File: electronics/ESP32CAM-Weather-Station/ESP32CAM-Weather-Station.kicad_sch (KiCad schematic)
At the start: 63 parts, among them IC1 BME688, IC2 SGP41-D-R4, IC3 VEML7700-TT, IC4 BQ24093DGQR, IC5 BQ29707DSET, IC6 MCP3426A0T-E_SN, IC7 TPS63070RNMR, J1 B4B-PH-SM4-TB_LF__SN_, J10 Conn_01x02_Pin, J2 B4B-PH-SM4-TB_LF__SN_, J3 B4B-PH-SM4-TB_LF__SN_, J4 B4B-PH-SM4-TB_LF__SN_, J5 B4B-PH-SM4-TB_LF__SN_, J6 XT30UPB-M, J7 Conn_01x02_Pin, J9 Conn_01x02_Pin, Q1 SIHLL110TR-GE3, Q2 CSD16406Q3, Q3 CSD16406Q3, U1 ESP32-CAM, U2 TPS631000DRLR

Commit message: [WIP] Added transient protection and mounting holes.
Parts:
- added D10, D11, D12, D13, D6, D7, D8, D9: ESDZV5H-1BU2, ESDZV5H-1BU2:ESDZV5H1BU2, symbol ESDZV5H-1BU2:ESDZV5H-1BU2
- added D5: SMBJ20CA-TR, SMBJ20CA-TR:DIONM5436X265N, symbol SMBJ20CA-TR:SMBJ20CA-TR
- added H2, H3, H4, H6: MountingHole, MountingHole:MountingHole_3.2mm_M3_Pad_Via, symbol Mechanical:MountingHole
- added H5: MountingHole_Pad, MountingHole:MountingHole_3.2mm_M3_DIN965_Pad, symbol Mechanical:MountingHole_Pad
- added J8: Conn_01x02_Pin, Connector_PinHeader_2.54mm:PinHeader_1x02_P2.54mm_Vertical, symbol Connector:Conn_01x02_Pin
- added U3: GDT25-07-S1-RP, GDT25-07-S1-RP:GDT2507S1RP, symbol GDT25-07-S1-RP:GDT25-07-S1-RP
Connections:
- net +3.3V: now also D10.2, D6.2, D7.2, D8.2
- net +VBAT: now also D13.2
- net +VBAT_UNFUSED: now also J8.1 (Pin_1)
- net GND: now also J6.N, D10.1, D11.1, D12.1, D13.1, D5.2, D6.1, D7.1, D8.1, D9.2, H5.1, J8.2 (Pin_2), U3.2
- net I2C_SDA: now also D11.2, D12.2
- net +VSOLAR: now reaches J6.P
- net +VSOLAR: now also R5.2, D5.1, U3.1
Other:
- note added: "Direct Battery and Solar Regulator Bypass"
- note added: "I2C Pullups and Protection"
- note added: "Mounting Holes and Earthing"
- note added: "Solar Protection"
- note removed: "Direct Battery and LDO Input Connection"
- note removed: "I2C Pullups"
- moved on the sheet: F1, H1, IC3, IC6, IC7, J10, J6, J9, R10, R11, R12, R13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

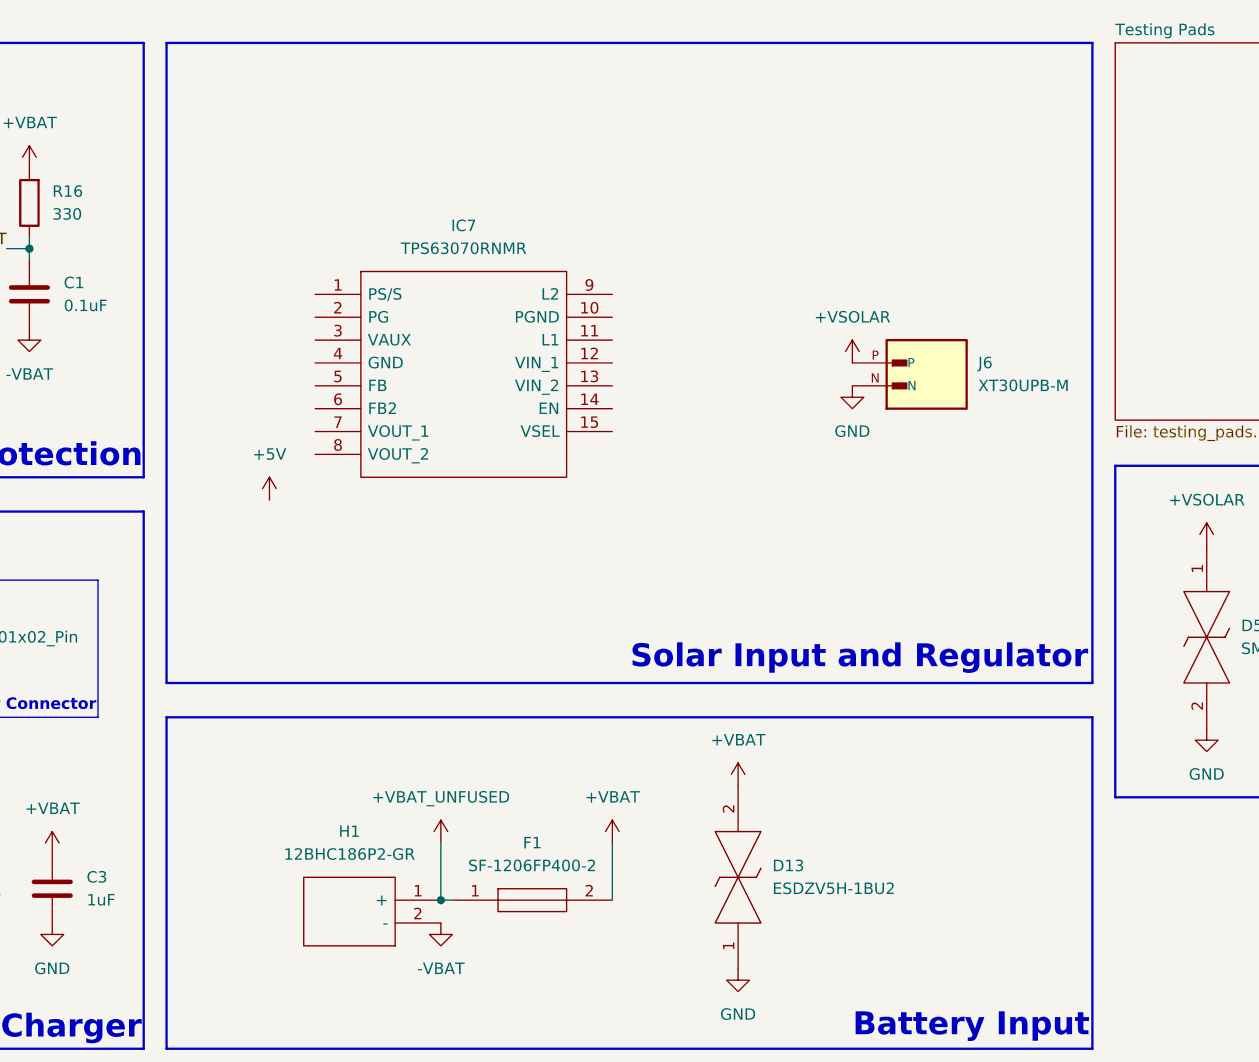
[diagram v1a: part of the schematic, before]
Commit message: [WIP] Routed solar input regulator.
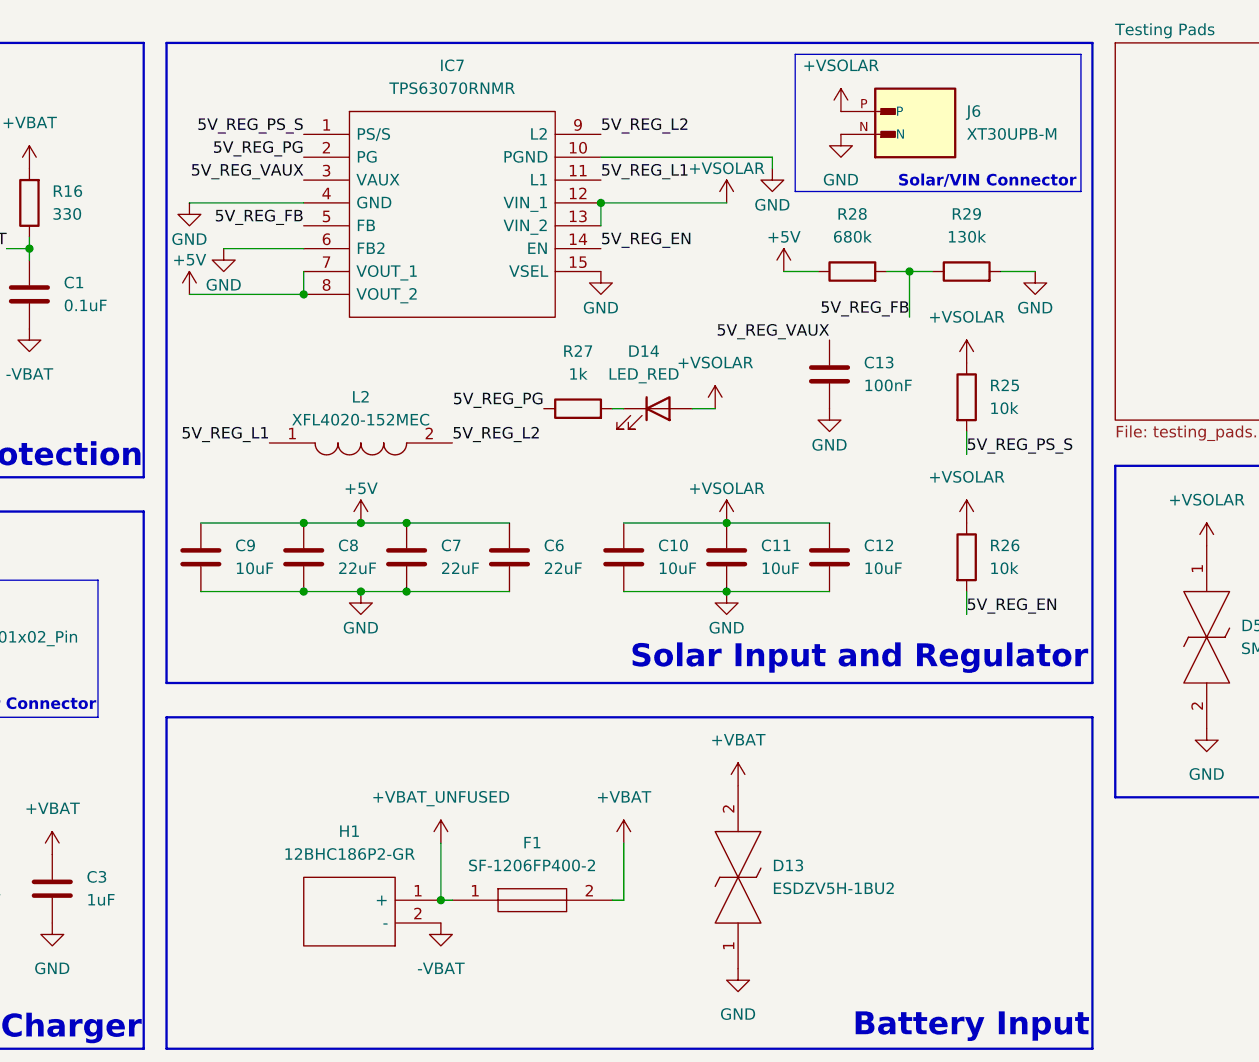
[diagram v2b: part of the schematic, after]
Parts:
- added C10, C9: 10uF, Capacitor_SMD:C_0603_1608Metric_Pad1.08x0.95mm_HandSolder, symbol Device:C
- added C11, C12: 10uF, Capacitor_SMD:C_0805_2012Metric_Pad1.18x1.45mm_HandSolder, symbol Device:C
- added C13: 100nF, Capacitor_SMD:C_0603_1608Metric_Pad1.08x0.95mm_HandSolder, symbol Device:C
- added C6, C7, C8: 22uF, Capacitor_SMD:C_0805_2012Metric_Pad1.18x1.45mm_HandSolder, symbol Device:C
- added D14: LED_RED, LED_SMD:LED_0805_2012Metric_Pad1.15x1.40mm_HandSolder, symbol Device:LED
- added L2: XFL4020-152MEC, XFL4020152MEC, symbol XFL4020-152MEC:XFL4020-152MEC
- added R25, R26: 10k, Resistor_SMD:R_0805_2012Metric_Pad1.20x1.40mm_HandSolder, symbol Device:R
- added R27: 1k, Resistor_SMD:R_0805_2012Metric_Pad1.20x1.40mm_HandSolder, symbol Device:R
- added R28: 680k, Resistor_SMD:R_0805_2012Metric_Pad1.20x1.40mm_HandSolder, symbol Device:R
- added R29: 130k, Resistor_SMD:R_0805_2012Metric_Pad1.20x1.40mm_HandSolder, symbol Device:R
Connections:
- net +5V: now also IC7.7 (VOUT_1), IC7.8 (VOUT_2), C6.1, C7.1, C8.1, C9.1, R28.1
- net +VSOLAR: now also IC7.12 (VIN_1), IC7.13 (VIN_2), C10.1, C11.1, C12.1, D14.2 (A), R25.1, R26.1
- net GND: now also IC7.10 (PGND), IC7.15 (VSEL), IC7.4 (GND), IC7.6 (FB2), C10.2, C11.2, C12.2, C13.1, C6.2, C7.2, C8.2, C9.2, R29.2
- net 5V_REG_PS_S: now reaches IC7.1 (PS/S)
- net 5V_REG_PS_S: now also R25.2
- net 5V_REG_L1: now reaches IC7.11 (L1)
- net 5V_REG_L1: now also L2.1
- net 5V_REG_EN: now reaches IC7.14 (EN)
- net 5V_REG_EN: now also R26.2
- net 5V_REG_PG: now reaches IC7.2 (PG)
- net 5V_REG_PG: now also R27.1
- net 5V_REG_VAUX: now reaches IC7.3 (VAUX)
- net 5V_REG_VAUX: now also C13.2
- net 5V_REG_FB: now reaches IC7.5 (FB)
- net 5V_REG_FB: now also R28.2, R29.1
- net 5V_REG_L2: now reaches IC7.9 (L2)
- net 5V_REG_L2: now also L2.2
- new net: D14.1 (K), R27.2
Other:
- note added: "Solar/VIN Connector"
- moved on the sheet: IC7, J6

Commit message: [WIP] Routed ADC and buzzer.
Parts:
- added C14: 10uF, Capacitor_SMD:C_0805_2012Metric_Pad1.18x1.45mm_HandSolder, symbol Device:C
- added C15: 100nF, Capacitor_SMD:C_0603_1608Metric_Pad1.08x0.95mm_HandSolder, symbol Device:C
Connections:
- net +3.3V: now also D9.1, IC6.3 (VDD), LS1.1 (+), C14.1, C15.2
- net GND: now also IC6.2 (CH1-), IC6.6 (VSS), IC6.8 (CH2-), Q1.3 (S), C14.2, C15.1
- net I2C_SCL: now also IC6.5 (SCL)
- net I2C_SDA: now also IC6.4 (SDA)
- net VBAT_SNS: now also IC6.1 (CH1+)
- net VSOLAR_SNS: now also IC6.7 (CH2+)
- net BUZZER_N: now reaches LS1.2 (-)
- net BUZZER_N: now also Q1.2 (D_1), Q1.4 (D_2)
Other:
- moved on the sheet: D1, D2, D6, IC6, JP1, JP2, JP3, R1, R2

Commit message: [WIP] Routed light sensor.
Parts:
- added C16: 10uF, Capacitor_SMD:C_0805_2012Metric_Pad1.18x1.45mm_HandSolder, symbol Device:C
- added C17: 100nF, Capacitor_SMD:C_0603_1608Metric_Pad1.08x0.95mm_HandSolder, symbol Device:C
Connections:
- net +3.3V: now also IC3.2 (VDD), C16.1, C17.2
- net GND: now also IC3.3 (GND), C16.2, C17.1
- net I2C_SCL: now also IC3.1 (SCL)
- net I2C_SDA: now also IC3.4 (SDA)
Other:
- moved on the sheet: D9

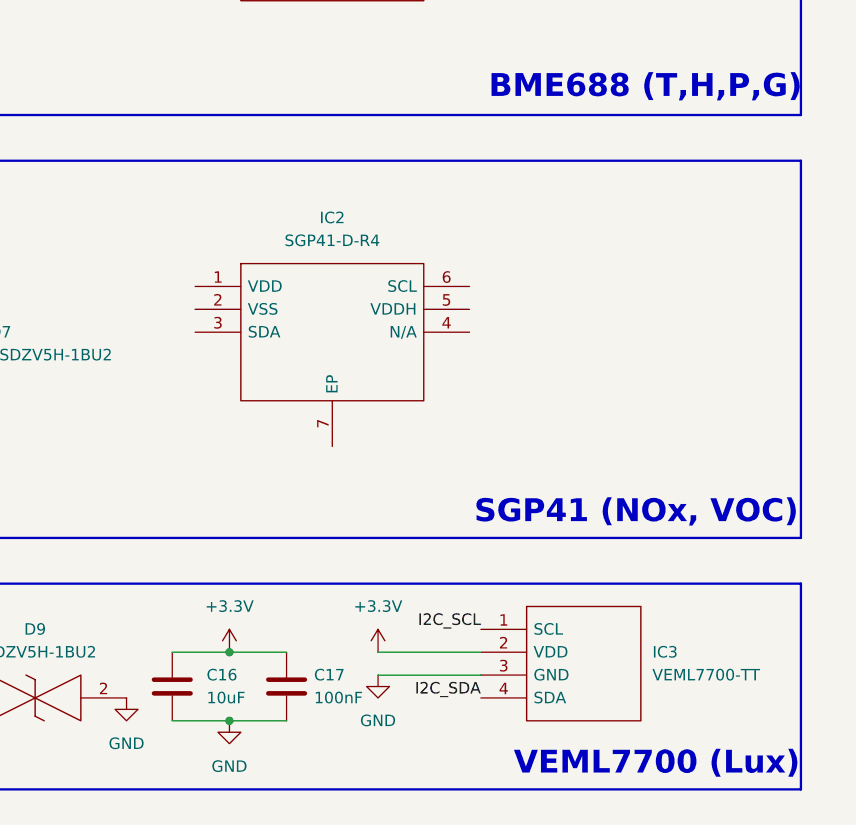
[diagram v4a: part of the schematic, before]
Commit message: [WIP] Routed SGP41.
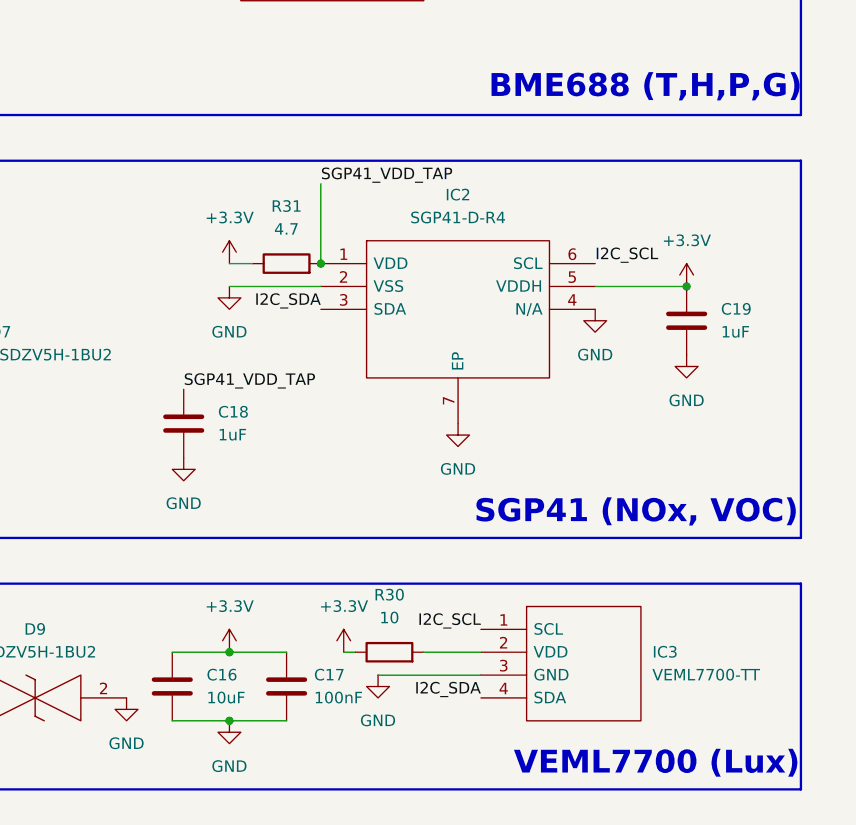
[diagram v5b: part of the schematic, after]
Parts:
- added C18, C19: 1uF, Capacitor_SMD:C_0805_2012Metric_Pad1.18x1.45mm_HandSolder, symbol Device:C
- added R30: 10, Resistor_SMD:R_0805_2012Metric_Pad1.20x1.40mm_HandSolder, symbol Device:R
- added R31: 4.7, Resistor_SMD:R_0805_2012Metric_Pad1.20x1.40mm_HandSolder, symbol Device:R
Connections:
- net +3.3V: now also IC2.5 (VDDH), C19.1, R30.1, R31.1; no longer IC3.2 (VDD)
- net GND: now also IC2.2 (VSS), IC2.4 (N/A), IC2.7 (EP), C18.2, C19.2
- net I2C_SCL: now also IC2.6 (SCL)
- net I2C_SDA: now also IC2.3 (SDA)
- net SGP41_VDD_TAP: now reaches IC2.1 (VDD)
- net SGP41_VDD_TAP: now also C18.1, R31.2
- new net: IC3.2 (VDD), R30.2
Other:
- moved on the sheet: IC2

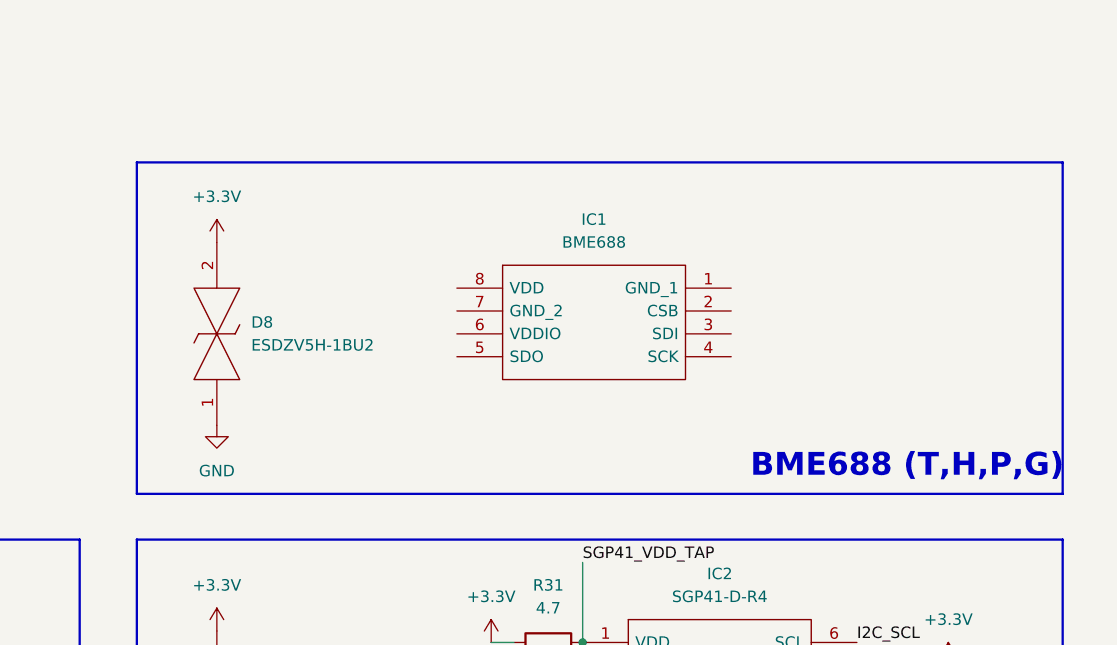
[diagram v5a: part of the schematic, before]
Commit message: [WIP] Routed BME688.
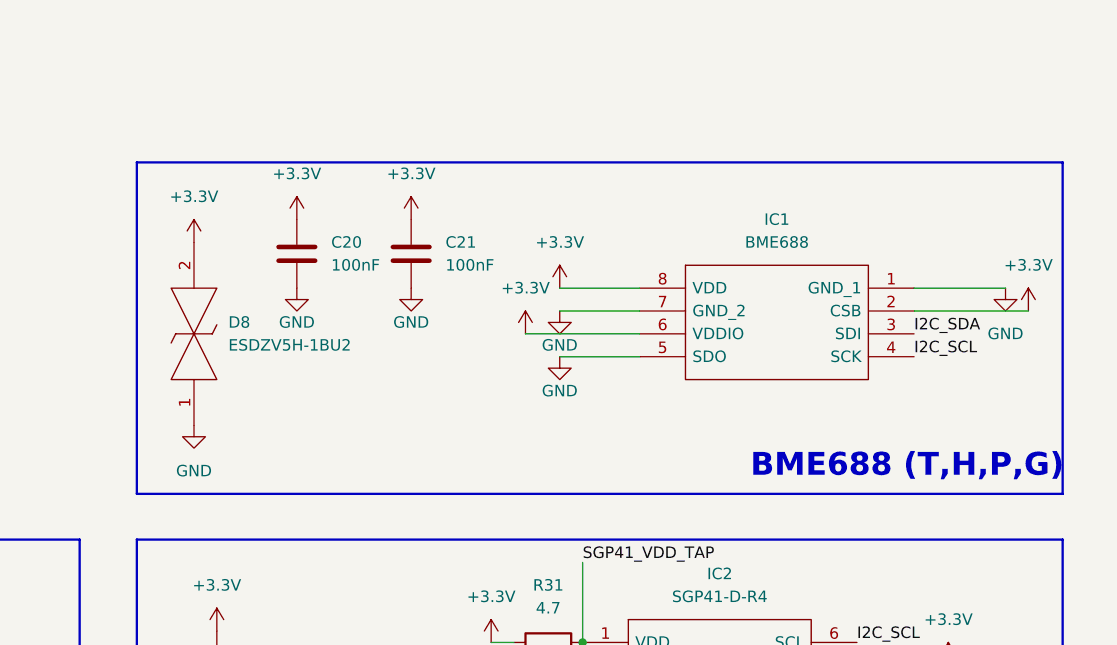
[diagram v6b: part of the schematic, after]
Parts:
- added C20, C21: 100nF, Capacitor_SMD:C_0603_1608Metric_Pad1.08x0.95mm_HandSolder, symbol Device:C
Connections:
- net +3.3V: now also IC1.2 (CSB), IC1.6 (VDDIO), IC1.8 (VDD), C20.2, C21.2
- net GND: now also IC1.1 (GND_1), IC1.5 (SDO), IC1.7 (GND_2), C20.1, C21.1
- net I2C_SCL: now also IC1.4 (SCK)
- net I2C_SDA: now also IC1.3 (SDI)
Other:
- moved on the sheet: D8, IC1

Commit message: [Ready for review] Final schematic housekeeping. Removed unusable I/O due to pin constraints (camera and SD)
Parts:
- removed D1, D2: LED_RED, LED_SMD:LED_0805_2012Metric_Pad1.15x1.40mm_HandSolder, symbol Device:LED
- removed J5: B4B-PH-SM4-TB_LF__SN_, B4B-PH-SM4-TB_LF__SN_:B4B-PH-SM4_1, symbol B4B-PH-SM4-TB_LF__SN_:B4B-PH-SM4-TB_LF__SN_
- removed JP1, JP2, JP3: SolderJumper_3_Open, symbol Jumper:SolderJumper_3_Open
- removed LS1: CMT-7525-80-SMT-TR, CMT-7525-80-SMT-TR:CMT752580SMTTR, symbol CMT-7525-80-SMT-TR:CMT-7525-80-SMT-TR
- removed Q1: SIHLL110TR-GE3, SIHLL110TR-GE3:SOT230P700X180-4N, symbol SIHLL110TR-GE3:SIHLL110TR-GE3
- removed R1, R2: 1k, Resistor_SMD:R_0805_2012Metric_Pad1.20x1.40mm_HandSolder, symbol Device:R
- removed R15: 47, Resistor_SMD:R_0805_2012Metric_Pad1.20x1.40mm_HandSolder, symbol Device:R
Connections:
- net GPIO1 is gone; now on net I2C_SDA: J4.4, U1.P$10 (IO1/U0T)
- net I2C_SCL: now also J4.3
- net I2C_SDA: no longer U1.P$15 (IO16)
- net GPIO0: no longer names the net of U1.P$14 (IO0)
- net GPIO0: no longer J4.3
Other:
- note removed: "Indicators"
- moved on the sheet: C14, C15, C18, C19, C20, C21, D10, D11, D12, D5, D6, D7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
